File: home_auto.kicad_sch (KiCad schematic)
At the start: 0 parts

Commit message: relay unit
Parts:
- added J1, J2, J3, J6, J7, J8: TC0203620000G, TC0203620000G, symbol TC0203620000G:TC0203620000G
- added J4, J5: Conn_02x10_Top_Bottom, Connector_PinHeader_2.54mm:PinHeader_2x10_P2.54mm_Vertical_SMD, symbol Connector_Generic:Conn_02x10_Top_Bottom
- added J9: Conn_01x08_Pin, Connector_PinHeader_1.27mm:PinHeader_1x08_P1.27mm_Vertical, symbol Connector:Conn_01x08_Pin
- added R1, R10, R11, R12, R13, R14, R16, R17, R19, R2, R20, R21, R22, R3, R4, R5, R6, R7, R8, R9: 4K7, Resistor_SMD:R_0603_1608Metric, symbol Device:R
- added R15: 0R, Resistor_SMD:R_0805_2012Metric, symbol Device:R
- added R18: 0R, Resistor_SMD:R_0603_1608Metric, symbol Device:R
- added U1: MACHox5_board, machox5_board:machox5_board, symbol machox5_board:MACHox5_board
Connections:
- new net +1V8: U1.B17 (1V8)
- new net +3V3: J9.1 (Pin_1), R15.1, U1.B16 (3V3)
- new net +5V: U1.B18 (5V), U1.B19 (5V)
- new net +UP: R1.2, R10.2, R11.2, R12.2, R13.2, R14.2, R15.2, R16.2, R17.2, R18.2, R19.2, R2.2, R20.2, R21.2, R22.2, R3.2, R4.2, R5.2, R6.2, R7.2, R8.2, R9.2
- new net 230VAC: J1.1, J1.2, J2.1, J2.2, J3.1, J3.2, J6.1, J6.2, J7.1, J7.2, J8.1, J8.2
- new net DOWN0: U1.F19 (GPIO73)
- new net DOWN1: U1.F15 (GPIO69)
- new net DOWN2: U1.F11 (GPIO65)
- new net DOWN3: U1.E7 (GPIO61)
- new net DOWN4: U1.E3 (GPIO57)
- new net DOWN_10: U1.C6 (GPIO20)
- new net DOWN_11: U1.C2 (GPIO16)
- new net DOWN_12: U1.C18 (GPIO32)
- new net DOWN_13: U1.C14 (GPIO28)
- new net DOWN_14: U1.C10 (GPIO24)
- new net GND: J9.8 (Pin_8), R18.1, U1.B0 (GND), U1.B1 (GND)
- new net RX: U1.B11 (GPIO9)
- new net TX: U1.B13 (GPIO11)
- new net UP0: U1.F17 (GPIO71)
- new net UP1: U1.F13 (GPIO67)
- new net UP2: U1.E9 (GPIO63)
- new net UP3: U1.E5 (GPIO59)
- new net UP4: U1.E1 (GPIO55)
- new net UP_10: U1.C8 (GPIO22)
- new net UP_11: U1.C4 (GPIO18)
- new net UP_12: U1.C0 (GPIO14)
- new net UP_13: U1.C16 (GPIO30)
- new net UP_14: U1.C12 (GPIO26)
- new net led_cur_lim5/DOWN: U1.E0 (GPIO54)
- new net led_cur_lim5/UP: U1.E2 (GPIO56)
- new net led_cur_lim6/DOWN: U1.C9 (GPIO23)
- new net led_cur_lim6/UP: U1.C7 (GPIO21)
- new net led_cur_lim7/DOWN: U1.E6 (GPIO60)
- new net led_cur_lim7/UP: U1.E8 (GPIO62)
- new net led_cur_lim8/DOWN: U1.C19 (GPIO33)
- new net led_cur_lim8/UP: U1.C17 (GPIO31)
- new net mux_0: J9.5 (Pin_5), U1.B5 (GPIO3)
- new net mux_1: J9.4 (Pin_4), U1.B6 (GPIO4)
- new net mux_2: J9.3 (Pin_3), U1.B7 (GPIO5)
- new net mux_3: J9.2 (Pin_2), U1.B8 (GPIO6)
- new net mux_4: J9.7 (Pin_7), U1.B3 (GPIO1)
- new net mux_5: J9.6 (Pin_6), U1.B4 (GPIO2)
- new net sw_0: J5.7 (Pin_7), J5.8 (Pin_8), R2.1, U1.D10 (GPIO44)
- new net sw_1: J5.5 (Pin_5), J5.6 (Pin_6), R4.1, U1.D11 (GPIO45)
- new net sw_10: J4.7 (Pin_7), J4.8 (Pin_8), R1.1, U1.D0 (GPIO34)
- new net sw_11: J4.5 (Pin_5), J4.6 (Pin_6), R3.1, U1.D1 (GPIO35)
- new net sw_12: J4.3 (Pin_3), J4.4 (Pin_4), R5.1, U1.D2 (GPIO36)
- new net sw_13: J4.1 (Pin_1), J4.2 (Pin_2), R7.1, U1.D3 (GPIO37)
- new net sw_14: J4.10 (Pin_10), J4.9 (Pin_9), R9.1, U1.D4 (GPIO38)
- new net sw_15: J4.11 (Pin_11), J4.12 (Pin_12), R11.1, U1.D5 (GPIO39)
- new net sw_16: J4.13 (Pin_13), J4.14 (Pin_14), R13.1, U1.D6 (GPIO40)
- new net sw_17: J4.15 (Pin_15), J4.16 (Pin_16), R16.1, U1.D7 (GPIO41)
- new net sw_18: J4.17 (Pin_17), J4.18 (Pin_18), R19.1, U1.D8 (GPIO42)
- new net sw_19: J4.19 (Pin_19), J4.20 (Pin_20), R21.1, U1.D9 (GPIO43)
- new net sw_2: J5.3 (Pin_3), J5.4 (Pin_4), R6.1, U1.D12 (GPIO46)
- new net sw_3: J5.1 (Pin_1), J5.2 (Pin_2), R8.1, U1.D13 (GPIO47)
- new net sw_4: J5.10 (Pin_10), J5.9 (Pin_9), R10.1, U1.D14 (GPIO48)
- new net sw_5: J5.11 (Pin_11), J5.12 (Pin_12), R12.1, U1.D15 (GPIO49)
- new net sw_6: J5.13 (Pin_13), J5.14 (Pin_14), R14.1, U1.D16 (GPIO50)
- new net sw_7: J5.15 (Pin_15), J5.16 (Pin_16), R17.1, U1.D17 (GPIO51)
- new net sw_8: J5.17 (Pin_17), J5.18 (Pin_18), R20.1, U1.D18 (GPIO52)
- new net sw_9: J5.19 (Pin_19), J5.20 (Pin_20), R22.1, U1.D19 (GPIO53)
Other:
- removed sheet FPGA_machX05
- removed sheet power_supply
- added sheet ESP32 (ESP32.kicad_sch)
- added sheet led_cluster (led_cluster.kicad_sch)
- added sheet led_cluster1 (led_cluster.kicad_sch)
- added sheet led_cur_lim5 (led_cur_lim.kicad_sch)
- added sheet led_cur_lim6 (led_cur_lim.kicad_sch)
- added sheet led_cur_lim7 (led_cur_lim.kicad_sch)
- added sheet led_cur_lim8 (led_cur_lim.kicad_sch)

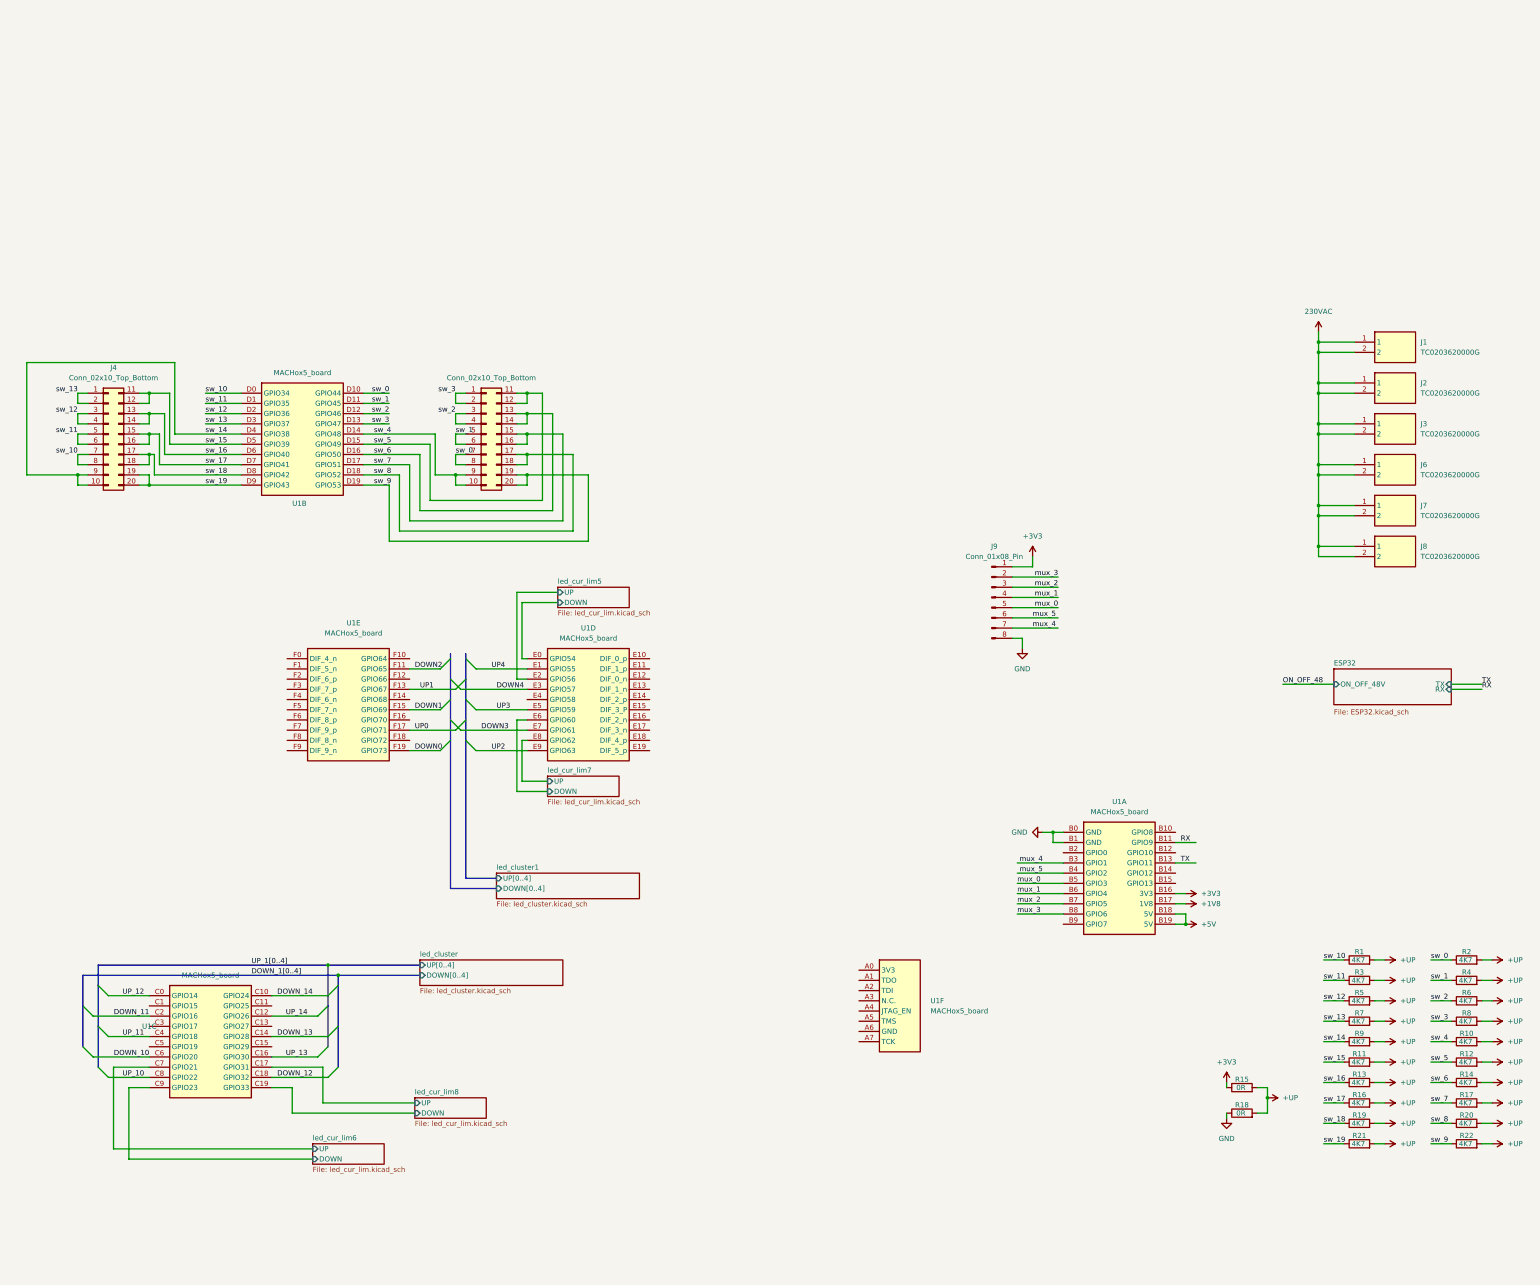
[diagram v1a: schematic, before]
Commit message: relay placment
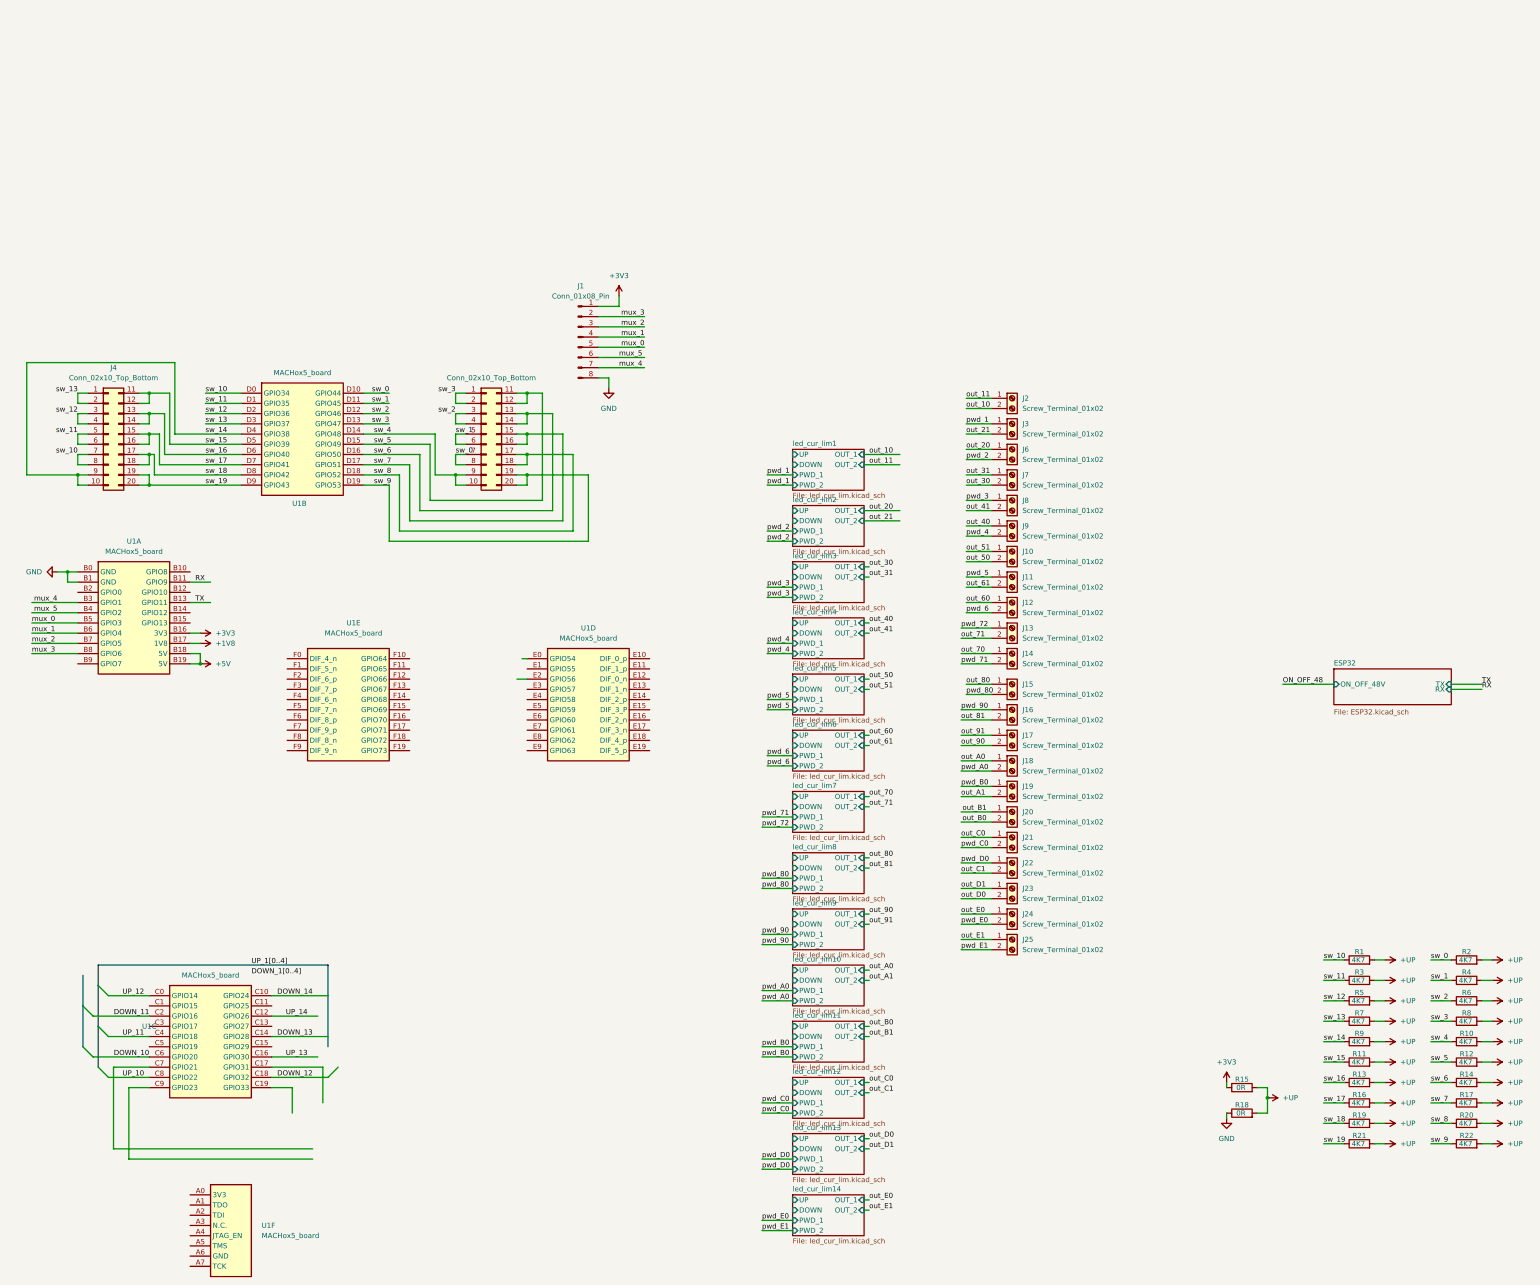
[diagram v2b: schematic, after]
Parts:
- removed J1, J2, J3, J6, J7, J8: TC0203620000G, TC0203620000G, symbol TC0203620000G:TC0203620000G
- added J10, J11, J12, J13, J14, J15, J16, J17, J18, J19, J2, J20, J21, J22, J23, J24, J25, J3, J6, J7, J8, J9: Screw_Terminal_01x02, KiCad:TC0203620000G, symbol Connector:Screw_Terminal_01x02
- J1: renamed from J9; footprint Connector_PinHeader_1.27mm:PinHeader_1x08_P1.27mm_Vertical -> Connector_PinHeader_2.54mm:PinHeader_1x08_P2.54mm_Vertical
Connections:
- net led_cur_lim5/DOWN: no longer U1.E0 (GPIO54)
- net led_cur_lim5/UP: no longer U1.E2 (GPIO56)
- net led_cur_lim6/DOWN: no longer U1.C9 (GPIO23)
- net led_cur_lim6/UP: no longer U1.C7 (GPIO21)
- net led_cur_lim7/DOWN: no longer U1.E6 (GPIO60)
- net led_cur_lim7/UP: no longer U1.E8 (GPIO62)
- net led_cur_lim8/DOWN: no longer U1.C19 (GPIO33)
- net led_cur_lim8/UP: no longer U1.C17 (GPIO31)
- net DOWN0: no longer names the net of U1.F19 (GPIO73)
- net DOWN1: no longer names the net of U1.F15 (GPIO69)
- net DOWN2: no longer names the net of U1.F11 (GPIO65)
- net DOWN3: no longer names the net of U1.E7 (GPIO61)
- net DOWN4: no longer names the net of U1.E3 (GPIO57)
- net UP0: no longer names the net of U1.F17 (GPIO71)
- net UP1: no longer names the net of U1.F13 (GPIO67)
- net UP2: no longer names the net of U1.E9 (GPIO63)
- net UP3: no longer names the net of U1.E5 (GPIO59)
- net UP4: no longer names the net of U1.E1 (GPIO55)
- new net out_10: J2.2 (Pin_2)
- new net out_11: J2.1 (Pin_1)
- new net out_20: J6.1 (Pin_1)
- new net out_21: J3.2 (Pin_2)
- new net out_30: J7.2 (Pin_2)
- new net out_31: J7.1 (Pin_1)
- new net out_40: J9.1 (Pin_1)
- new net out_41: J8.2 (Pin_2)
- new net out_50: J10.2 (Pin_2)
- new net out_51: J10.1 (Pin_1)
- new net out_60: J12.1 (Pin_1)
- new net out_61: J11.2 (Pin_2)
- new net out_70: J14.1 (Pin_1)
- new net out_71: J13.2 (Pin_2)
- new net out_80: J15.1 (Pin_1)
- new net out_81: J16.2 (Pin_2)
- new net out_90: J17.2 (Pin_2)
- new net out_91: J17.1 (Pin_1)
- new net out_A0: J18.1 (Pin_1)
- new net out_A1: J19.2 (Pin_2)
- new net out_B0: J20.2 (Pin_2)
- new net out_B1: J20.1 (Pin_1)
- new net out_C0: J21.1 (Pin_1)
- new net out_C1: J22.2 (Pin_2)
- new net out_D0: J23.2 (Pin_2)
- new net out_D1: J23.1 (Pin_1)
- new net out_E0: J24.1 (Pin_1)
- new net out_E1: J25.1 (Pin_1)
- new net pwd_1: J3.1 (Pin_1)
- new net pwd_2: J6.2 (Pin_2)
- new net pwd_3: J8.1 (Pin_1)
- new net pwd_4: J9.2 (Pin_2)
- new net pwd_5: J11.1 (Pin_1)
- new net pwd_6: J12.2 (Pin_2)
- new net pwd_71: J14.2 (Pin_2)
- new net pwd_72: J13.1 (Pin_1)
- new net pwd_80: J15.2 (Pin_2)
- new net pwd_90: J16.1 (Pin_1)
- new net pwd_A0: J18.2 (Pin_2)
- new net pwd_B0: J19.1 (Pin_1)
- new net pwd_C0: J21.2 (Pin_2)
- new net pwd_D0: J22.1 (Pin_1)
- new net pwd_E0: J24.2 (Pin_2)
- new net pwd_E1: J25.2 (Pin_2)
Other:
- removed sheet led_cluster
- removed sheet led_cluster1
- added sheet led_cur_lim1 (led_cur_lim.kicad_sch)
- added sheet led_cur_lim10 (led_cur_lim.kicad_sch)
- added sheet led_cur_lim11 (led_cur_lim.kicad_sch)
- added sheet led_cur_lim12 (led_cur_lim.kicad_sch)
- added sheet led_cur_lim13 (led_cur_lim.kicad_sch)
- added sheet led_cur_lim14 (led_cur_lim.kicad_sch)
- added sheet led_cur_lim2 (led_cur_lim.kicad_sch)
- added sheet led_cur_lim3 (led_cur_lim.kicad_sch)
- added sheet led_cur_lim4 (led_cur_lim.kicad_sch)
- added sheet led_cur_lim9 (led_cur_lim.kicad_sch)
- sheet led_cur_lim5 ports: added OUT_1, OUT_2, PWD_1, PWD_2; removed none
- sheet led_cur_lim6 ports: added OUT_1, OUT_2, PWD_1, PWD_2; removed none
- sheet led_cur_lim7 ports: added OUT_1, OUT_2, PWD_1, PWD_2; removed none
- sheet led_cur_lim8 ports: added OUT_1, OUT_2, PWD_1, PWD_2; removed none
- moved on the sheet: J1, U1A, U1F

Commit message: filse fo JCL pcb generated
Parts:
- renumbered R16 to R15, R17 to R16, R19 to R17, R20 to R18, R21 to R19, R22 to R20, R15 to R21, R18 to R22
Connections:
- net RX: now also U1.B13 (GPIO11); no longer U1.B11 (GPIO9)
- net TX: now also U1.B11 (GPIO9); no longer U1.B13 (GPIO11)
- net sw_0: now also J5.19 (Pin_19), J5.20 (Pin_20), R1.1, U1.D0 (GPIO34); no longer J5.7 (Pin_7), J5.8 (Pin_8), R2.1, U1.D10 (GPIO44)
- net sw_1: now also J4.19 (Pin_19), J4.20 (Pin_20), R2.1, U1.D1 (GPIO35); no longer J5.5 (Pin_5), J5.6 (Pin_6), R4.1, U1.D11 (GPIO45)
- net sw_10: now also J4.10 (Pin_10), J4.9 (Pin_9), R11.1, U1.D10 (GPIO44); no longer J4.7 (Pin_7), J4.8 (Pin_8), R1.1, U1.D0 (GPIO34)
- net sw_11: now also J5.10 (Pin_10), J5.9 (Pin_9), R12.1, U1.D11 (GPIO45); no longer J4.5 (Pin_5), J4.6 (Pin_6), R3.1, U1.D1 (GPIO35)
- net sw_12: now also J4.7 (Pin_7), J4.8 (Pin_8), R13.1, U1.D12 (GPIO46); no longer J4.3 (Pin_3), J4.4 (Pin_4), R5.1, U1.D2 (GPIO36)
- net sw_13: now also J5.7 (Pin_7), J5.8 (Pin_8), R14.1, U1.D13 (GPIO47); no longer J4.1 (Pin_1), J4.2 (Pin_2), R7.1, U1.D3 (GPIO37)
- net sw_14: now also J4.5 (Pin_5), J4.6 (Pin_6), R15.1, U1.D14 (GPIO48); no longer J4.10 (Pin_10), J4.9 (Pin_9), R9.1, U1.D4 (GPIO38)
- net sw_15: now also J5.5 (Pin_5), J5.6 (Pin_6), R16.1, U1.D15 (GPIO49); no longer J4.11 (Pin_11), J4.12 (Pin_12), R11.1, U1.D5 (GPIO39)
- net sw_16: now also J4.3 (Pin_3), J4.4 (Pin_4), R17.1, U1.D16 (GPIO50); no longer J4.13 (Pin_13), J4.14 (Pin_14), R13.1, U1.D6 (GPIO40)
- net sw_17: now also J5.3 (Pin_3), J5.4 (Pin_4), R18.1, U1.D17 (GPIO51); no longer J4.15 (Pin_15), J4.16 (Pin_16), R15.1, U1.D7 (GPIO41)
- net sw_18: now also J4.1 (Pin_1), J4.2 (Pin_2), R19.1, U1.D18 (GPIO52); no longer J4.17 (Pin_17), J4.18 (Pin_18), R17.1, U1.D8 (GPIO42)
- net sw_19: now also J5.1 (Pin_1), J5.2 (Pin_2), R20.1, U1.D19 (GPIO53); no longer J4.19 (Pin_19), J4.20 (Pin_20), R19.1, U1.D9 (GPIO43)
- net sw_2: now also J5.17 (Pin_17), J5.18 (Pin_18), R3.1, U1.D2 (GPIO36); no longer J5.3 (Pin_3), J5.4 (Pin_4), R6.1, U1.D12 (GPIO46)
- net sw_3: now also J4.17 (Pin_17), J4.18 (Pin_18), R4.1, U1.D3 (GPIO37); no longer J5.1 (Pin_1), J5.2 (Pin_2), R8.1, U1.D13 (GPIO47)
- net sw_4: now also J5.15 (Pin_15), J5.16 (Pin_16), R5.1, U1.D4 (GPIO38); no longer J5.10 (Pin_10), J5.9 (Pin_9), R10.1, U1.D14 (GPIO48)
- net sw_5: now also J4.15 (Pin_15), J4.16 (Pin_16), R6.1, U1.D5 (GPIO39); no longer J5.11 (Pin_11), J5.12 (Pin_12), R12.1, U1.D15 (GPIO49)
- net sw_6: now also R7.1, U1.D6 (GPIO40); no longer R14.1, U1.D16 (GPIO50)
- net sw_7: now also J4.13 (Pin_13), J4.14 (Pin_14), R8.1, U1.D7 (GPIO41); no longer J5.15 (Pin_15), J5.16 (Pin_16), R16.1, U1.D17 (GPIO51)
- net sw_8: now also J5.11 (Pin_11), J5.12 (Pin_12), R9.1, U1.D8 (GPIO42); no longer J5.17 (Pin_17), J5.18 (Pin_18), R18.1, U1.D18 (GPIO52)
- net sw_9: now also J4.11 (Pin_11), J4.12 (Pin_12), R10.1, U1.D9 (GPIO43); no longer J5.19 (Pin_19), J5.20 (Pin_20), R20.1, U1.D19 (GPIO53)
- net down_E: now reaches U1.E0 (GPIO54)
- net up_C: now reaches U1.E10 (DIF_0_p)
- net down_B: now reaches U1.E12 (DIF_0_n)
- net up_B: now reaches U1.E14 (DIF_2_p)
- net down_A: now reaches U1.E16 (DIF_2_n)
- net up_A: now reaches U1.E18 (DIF_4_p)
- net up_E: now reaches U1.E2 (GPIO56)
- net down_D: now reaches U1.E4 (GPIO58)
- net up_D: now reaches U1.E6 (GPIO60)
- net down_C: now reaches U1.E8 (GPIO62)
- net down_9: now reaches U1.F0 (DIF_4_n)
- net up_9: now reaches U1.F2 (DIF_6_p)
- net down_8: now reaches U1.F4 (DIF_6_n)
- net up_8: now reaches U1.F6 (DIF_8_p)
- net up_2: now reaches U1.C1 (GPIO15)
- net down_2: now reaches U1.C3 (GPIO17)
- net up_1: now reaches U1.C5 (GPIO19)
- net down_1: now reaches U1.C7 (GPIO21)
- net DOWN_10 renamed down_6
- net DOWN_11 renamed down_7
- net DOWN_12 renamed down_3
- net DOWN_13 renamed down_4
- net DOWN_14 renamed down_5
- net UP_10 renamed up_5
- net UP_11 renamed up_6
- net UP_12 renamed up_7
- net UP_13 renamed up_3
- net UP_14 renamed up_4
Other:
- moved on the sheet: J10, J11, J12, J13, J14, J15, J16, J17, J18, J19, J2, J20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
